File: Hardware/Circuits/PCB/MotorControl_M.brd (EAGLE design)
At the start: 72 x 150 mm, 71 parts, among them U1 LTC4359CMS8PBF, U2 SX1509, U3 MAX8881EUT50T

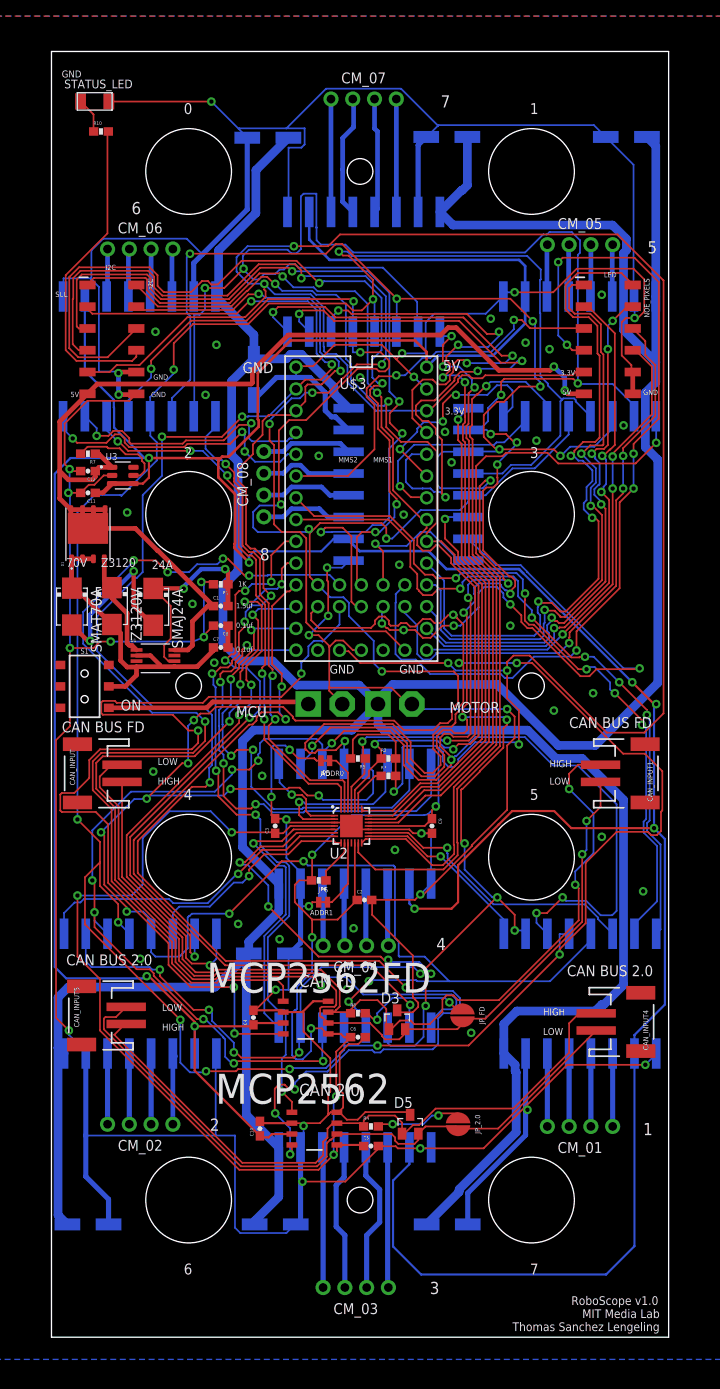
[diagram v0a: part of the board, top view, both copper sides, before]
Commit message: enable Motor
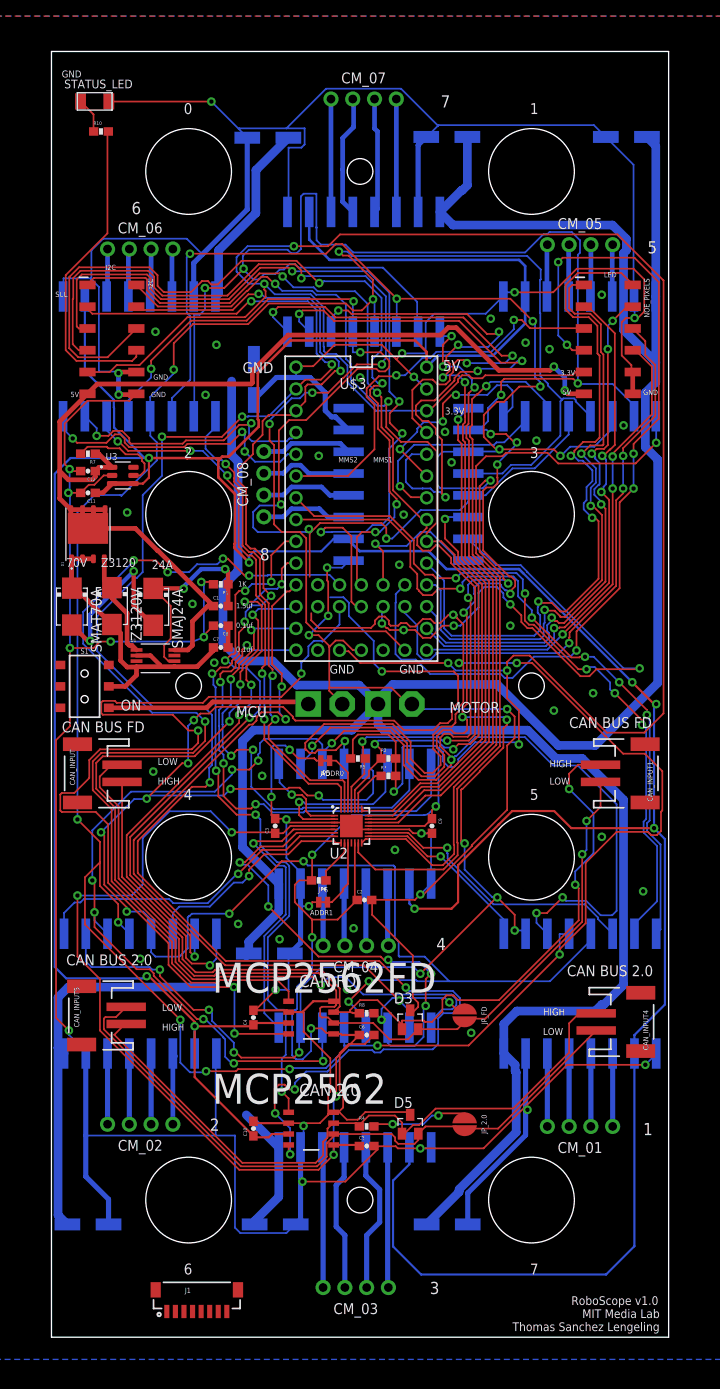
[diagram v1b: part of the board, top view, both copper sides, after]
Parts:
- added J1: (no value), SparkFun-Connectors:BM08B-SRSS-TB
- moved D3 1.52 mm to (43.9, 40.1)
- moved C6 1.05 mm to (38.9, 38.4)
- moved R8 1.02 mm to (38.9, 40.9)
- moved C10 0.76 mm to (25.7, 27.4)
- moved JP_2.0 0.76 mm to (50.3, 27.9)
- moved MCP2562FD 0.63 mm to (32.4, 40.4)
- moved C5 0.51 mm to (38.9, 25.4)
- moved R4 0.51 mm to (38.9, 27.7)
- moved MCP2562 0.38 mm to (32.4, 27.4)
- moved JP_FD 0.25 mm to (50.3, 40.6)
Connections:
- net GND_MCU: now also J1.1
- net INT_01: now also U$3.32; no longer U$3.28
- net INT_02: now also U$3.33; no longer U$3.29
- net SX00_1: now also J1.8
- net SX00_11: now also J1.3
- net SX00_3: now also J1.6
- net SX00_5: now also J1.5
- net SX00_7: now also J1.4
- net SX00_9: now also J1.7
- net TRQ1: now also U$3.28; no longer U$3.32
- net TRQ2: now also U$3.29; no longer U$3.33
- net VCC_5V: now also J1.2
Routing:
- net VCC_M: track 492.4 -> 441.6 mm
- net TRQ2: track 349.7 -> 346.3 mm
- net GND_MCU: track 758.4 -> 760.1 mm
- net N$3: track 9.94 -> 11.2 mm
- net 3.3V: track 468.5 -> 469.7 mm
- net TRQ1: track 394.2 -> 393.1 mm
- net CAN_L: track 109.0 -> 108.2 mm
- net INT_02: track 101.1 -> 100.4 mm
- net VCC_5VREG: track 468.5 -> 469.2 mm
- net CAN_RX3: track 117.4 -> 118.1 mm
- net INT_01: track 98.9 -> 98.3 mm
- net MSTEP_03: track 87.6 -> 87.0 mm
- net CAN_H: track 109.9 -> 110.4 mm

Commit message: update circuits
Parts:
- removed C11, C12: 4.7uf, SparkFun-Capacitors:0603-CAP
- removed I2C, NOE_PIXELS: (no value), SparkFun-Connectors:2X6_SMD
- removed JP_2.0, JP_FD: JUMPER-SMT_2_NO_NO-SILK_ROUND, SparkFun-Jumpers:SMT-JUMPER_2_NO_NO-SILK_ROUND
- removed MCP2562: MCP2562, MCP2562:MCP2562
- removed S1: (no value), SparkFun-Switches:SWITCH_DPDT_SMD_AYZ0202
- removed SMAJ24A, SMAT70A, Z3120V: S2M, s2x_10:DO214AA
- added D2: 3A/40V/500mV, SparkFun-DiscreteSemi:SMA-DIODE
- added J2, J3: (no value), SparkFun-Connectors:1X02
- added J4: (no value), SparkFun-Connectors:1X06-1MM
- added JP1, JP2: JUMPER-SMT_2_NC_TRACE_NO-SILK, SparkFun-Jumpers:SMT-JUMPER_2_NC_TRACE_NO-SILK
- added JP3, JP4, JP7: SMT_2, SparkFun-Jumpers:SMT-JUMPER_2_NC_TRACE_NO-SILK
- added JP8: SMT_2, SparkFun-Jumpers:SMT-JUMPER_2_NO_NO-SILK
- added MCP2562_2.0: MCP2562-E/SN, MCP2562-E_SN:SOIC127P600X175-8N
- added P1: M-2X10-87759, con-headers-jp:87759-20
- added R11, R9: 10K, SparkFun-Resistors:0603-RES
- added R12, R13, R14, R15, R16, R17, R18, R19: 100, SparkFun-Resistors:0805
- added U$1: MOSFET_SLIDER, Mosfet_slider:MOSFET_SLIDER
- C1: value 1.5uf -> 47uf/10V
- D1: value BSC010NE2LSI -> S2A; device BSC010NE2LSI:SOFL127P515X615X110-9N -> s2x_10:DO214AA
- J1: device SparkFun-Connectors:BM08B-SRSS-TB -> SparkFun-Connectors:1X06-1MM
- MCP2562FD: value MCP2562 -> MCP2562-E/SN; device MCP2562:MCP2562 -> MCP2562-E_SN:SOIC127P600X175-8N
- R1: value 1K -> 0.3; device SparkFun-Resistors:0603-RES -> SparkFun-Resistors:0805
- R7: value 100K -> 120Ohms
- U1: value LTC4359CMS8PBF -> MIC2005; device LTC4359CMS8PBF:MSOP-8_MS -> Microchip:SOT23-6
- U3: value MAX8881EUT50T -> TEXAS_INSTRUMENTS_SN74HCT245DW; device MAX8881EUT50T:SOT95P280X145-6N -> Texas Instruments - SN74HCT245DW:74HCT245
- moved C8 154.8 mm to (-30.2, -59.7), turned to 0 degrees
- moved U3 127.2 mm to (121.7, 41.9)
- moved C1 118.6 mm to (-13.2, -24.9)
- moved C7 116.9 mm to (-13.2, -27.9)
- moved U1 79.9 mm to (-21.1, 10.7)
- moved R7 68.2 mm to (46.7, 51.2)
- moved J1 55.3 mm to (7.37, 60.2), flipped to the bottom, turned to 270 degrees
- moved STATUS_LED 55.2 mm to (62.3, 150.3), turned to 180 degrees
- moved R10 55.2 mm to (62.9, 147.7), turned to 180 degrees
- moved CAN_INPUT1 27.5 mm to (59.9, 43.2)
- moved CAN_INPUT 27.5 mm to (16.5, 43.2)
- moved D1 27.3 mm to (18.7, 72.4), turned to 270 degrees
- moved R1 19.4 mm to (15.7, 72.5), turned to 270 degrees
- moved CAN_INPUT5 11.2 mm to (16.5, 34.5)
- moved CAN_INPUT4 10.8 mm to (59.9, 34.5)
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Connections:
- removed net N$12: SMAJ24A.A, SMAT70A.A
- removed net TRQ1: MOTOR_01.1, MOTOR_02.1, MOTOR_03.1, MOTOR_04.1, MOTOR_05.1, MOTOR_06.1, MOTOR_07.1, MOTOR_08.1, U$3.28
- removed net TRQ2: MOTOR_01.2, MOTOR_02.2, MOTOR_03.2, MOTOR_04.2, MOTOR_05.2, MOTOR_06.2, MOTOR_07.2, MOTOR_08.2, U$3.29
- removed net VCC_5V: C1.1, C12.1, D1.5, D1.6, D1.7, D1.8, D1.9, I2C.11, J1.2, NOE_PIXELS.11, R7.1, U1.8, U3.1
- new net CLK_RX/STANBY: MOTOR_01.STBY, MOTOR_02.STBY, MOTOR_03.STBY, MOTOR_04.STBY, MOTOR_05.STBY, MOTOR_06.STBY, MOTOR_07.STBY, MOTOR_08.STBY, U$3.29
- new net N$10: R11.2, U1.4
- new net N$11: R12.2, U3.18
- new net N$13: R9.2, U1.3
- new net N$21: R13.2, U3.17
- new net N$22: R14.2, U3.16
- new net N$23: R15.2, U3.15
- new net N$25: R17.2, U3.13
- new net N$26: R18.2, U3.12
- new net N$27: R19.2, U3.11
- new net N$5: C6.1, JP1.1, MCP2562FD.5
- new net N$7: U$1.GND_5
- new net N$8: P1.16
- new net NEOPIXEL_01_5V: P1.1, R12.1
- new net NEOPIXEL_02_5V: P1.3, R13.1
- new net NEOPIXEL_03_5V: P1.5, R14.1
- new net NEOPIXEL_04_5V: P1.7, R15.1
- new net NEOPIXEL_05_5V: P1.9, R16.1
- new net NEOPIXEL_06_5V: P1.11, R17.1
- new net NEOPIXEL_07_5V: P1.13, R18.1
- new net NEOPIXEL_08_5V: P1.15, R19.1
- new net TRQ1_SPREAD: JP7.2, MOTOR_01.1, MOTOR_02.1, MOTOR_03.1, MOTOR_04.1, MOTOR_05.1, MOTOR_06.1, MOTOR_07.1, MOTOR_08.1
- new net TRQ2/UART: MOTOR_01.2, MOTOR_02.2, MOTOR_03.2, MOTOR_04.2, MOTOR_05.2, MOTOR_06.2, MOTOR_07.2, MOTOR_08.2, U$3.28
- new net VCC_LEDS: C1.1, C7.1, D1.C, D2.A, D2.C, P1.17, R1.1, U1.1
- net 3.3V: now also P1.19; no longer C5.1, C6.1, I2C.9, MCP2562.VIO, MCP2562FD.VIO, NOE_PIXELS.9
- net CAN_H: now also MCP2562FD.7; no longer MCP2562FD.CANH
- net CAN_H2: now also MCP2562_2.0.7; no longer MCP2562.CANH
- net CAN_L: now also J2.2, MCP2562FD.6; no longer JP_FD.2, MCP2562FD.CANL
- net CAN_L2: now also J3.2, MCP2562_2.0.6; no longer JP_2.0.2, MCP2562.CANL
- net CAN_RX2: now also MCP2562_2.0.4; no longer I2C.3, MCP2562.RXD
- net CAN_RX3: now also MCP2562FD.4; no longer MCP2562FD.RXD
- net CAN_TX2: now also MCP2562_2.0.1; no longer I2C.4, MCP2562.TXD
- net CAN_TX3: now also MCP2562FD.1; no longer MCP2562FD.TXD
- net GND_MCU: now also C1.2, C7.2, D1.A, J4.1, MCP2562FD.2, MCP2562FD.8, MCP2562_2.0.2, MCP2562_2.0.8, P1.18, P1.20, U$1.GND_1, U$1.GND_2, U$1.GND_3, U$1.GND_4, U1.2, U3.10, U3.19; no longer C11.2, C12.2, I2C.10, I2C.12, MCP2562.STBY, MCP2562.VSS, MCP2562FD.STBY, MCP2562FD.VSS, NOE_PIXELS.10, NOE_PIXELS.12, R1.2, U3.2
- net INT_01: now also P1.6; no longer I2C.5
- net INT_02: now also P1.8; no longer I2C.6
- net MMS1: now also JP4.2
- net MMS2: now also JP3.2, R7.1
- net N$1: now also J2.1; no longer JP_FD.1
- net N$2: now also JP8.1, U$1.ON; no longer D1.4, U1.1, Z3120V.C
- net N$3: now also J3.1; no longer JP_2.0.1
- net N$4: now also R16.2, U3.14; no longer C1.2, R1.1, SMAJ24A.C, U1.6
- net N$6: now also C5.1, JP2.1, MCP2562_2.0.5; no longer R7.2, U3.5
- net N$9: now also P1.14; no longer C7.2, C8.1
- net NEOPIXEL_01: now also U3.2; no longer NOE_PIXELS.1
- net NEOPIXEL_02: now also U3.3; no longer NOE_PIXELS.2
- net NEOPIXEL_03: now also U3.4; no longer NOE_PIXELS.3
- net NEOPIXEL_04: now also U3.5; no longer NOE_PIXELS.4
- net NEOPIXEL_05: now also U3.6; no longer NOE_PIXELS.5
- net NEOPIXEL_06: now also U3.7; no longer NOE_PIXELS.6
- net NEOPIXEL_07: now also U3.8; no longer NOE_PIXELS.7
- net NEOPIXEL_08: now also U3.9; no longer NOE_PIXELS.8
- net RESET: now also P1.10; no longer I2C.7
- net STATUS_PIN: now also P1.12; no longer I2C.8
- net SX00_1: now also J1.3; no longer J1.8, MOTOR_06.STBY
- net SX00_11: now also J4.4, JP4.1; no longer J1.3, MOTOR_01.STBY
- net SX00_13: now also J4.5, JP7.1; no longer MOTOR_07.STBY
- net SX00_15: now also J4.6, JP8.2; no longer MOTOR_08.STBY
- net SX00_3: now also J1.4; no longer J1.6, MOTOR_04.STBY
- net SX00_5: no longer MOTOR_03.STBY
- net SX00_7: now also J1.6; no longer J1.4, MOTOR_02.STBY
- net SX00_9: now also J4.3, JP3.1; no longer J1.7, MOTOR_05.STBY
- net SX00_SCL: now also P1.4; no longer I2C.1
- net SX00_SDA: now also P1.2; no longer I2C.2
- net VCC_5VREG: now also C8.1, J1.2, J4.2, JP1.2, JP2.2, MCP2562FD.3, MCP2562_2.0.3, R7.2, U1.6, U3.1, U3.20; no longer C11.1, MCP2562.VDD, MCP2562FD.VDD, U3.3, U3.4
- net VCC_MCU: now also U$1.VIN_1, U$1.VIN_2; no longer S1.3
- net VCC_SWITCH: now also R1.2, R11.1, R9.1, U$1.VOUT_1, U$1.VOUT_2; no longer C7.1, D1.1, D1.2, D1.3, S1.2, SMAT70A.C, U1.2, U1.4, U1.5, Z3120V.A
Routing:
- net TRQ1: track 393.1 -> 0.00 mm, vias 14 -> 0
- net TRQ2: track 346.3 -> 0.00 mm, vias 18 -> 0
- net CLK_RX/STANBY: track 0.00 -> 329.3 mm, vias 0 -> 9
- net TRQ2/UART: track 0.00 -> 317.0 mm, vias 0 -> 13
- net TRQ1_SPREAD: track 0.00 -> 305.2 mm, vias 0 -> 13
- net VCC_M: track 441.6 -> 717.2 mm
- net 3.3V: track 469.7 -> 245.9 mm, vias 14 -> 21
- net GND_MCU: track 760.1 -> 964.8 mm, vias 62 -> 33
- net VCC_5V: track 125.2 -> 0.00 mm, vias 2 -> 0
- net CAN_H: track 110.4 -> 40.1 mm, vias 2 -> 0
- net SX00_13: track 96.2 -> 35.4 mm, vias 5 -> 1
- net CAN_L: track 108.2 -> 48.4 mm, vias 2 -> 0
- net MSTEP_08: track 67.9 -> 12.8 mm, vias 5 -> 0
- net SX00_15: track 47.9 -> 100.2 mm, vias 1 -> 3
- net CAN_RX2: track 209.6 -> 158.0 mm, vias 9 -> 3
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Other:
- board size 72 x 150 mm -> 74.8 x 147 mm
- board text added: "CB 2.0"
- board text added: "CB FD"
- board text removed: "0.1uf"
- board text removed: "1.5uf"
- board text removed: "1K"
- board text removed: "24A"
- board text removed: "70V"
- board text removed: "CAN BUS 2.0"
- board text removed: "CAN BUS FD"
- board text removed: "MMS1"
- board text removed: "MMS2"
- board text removed: "Z3120"
